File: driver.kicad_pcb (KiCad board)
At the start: 2 copper layers, 25 x 20 mm, 29 parts, among them J1 FAN_TACH, J2 FAN_PWM, J3 HF1004E, Q1 BSS138, U1 MP2315SGJ-Z

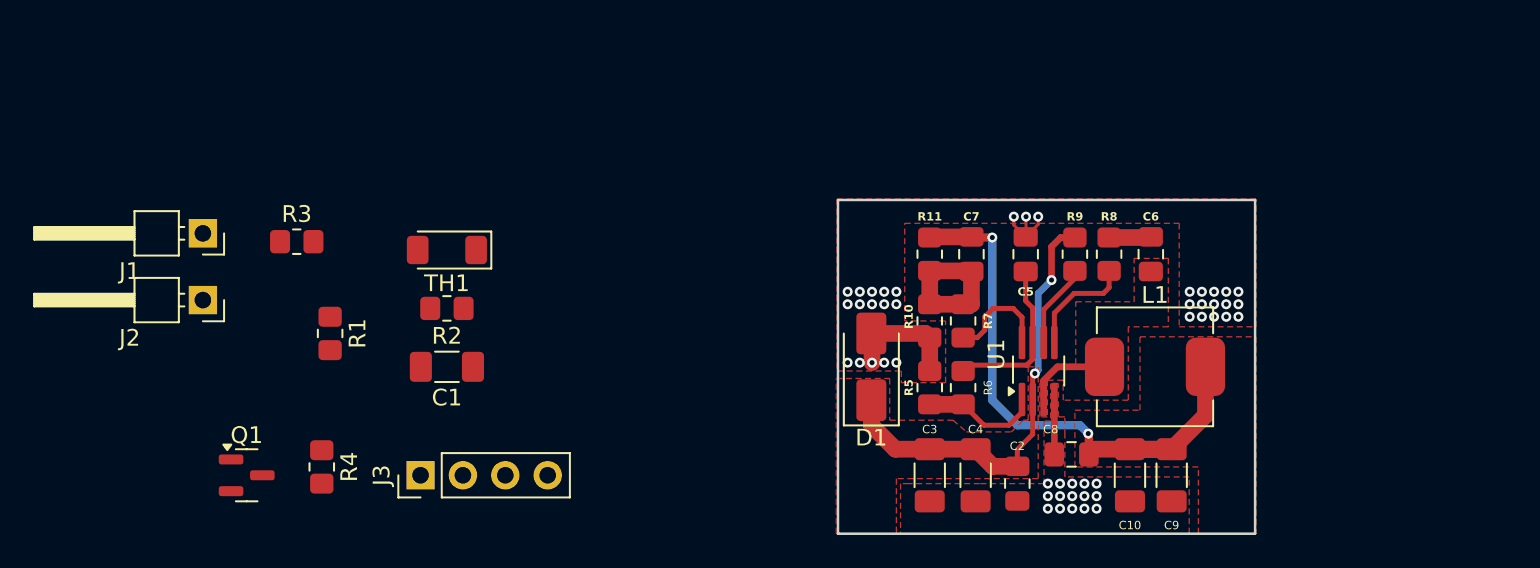
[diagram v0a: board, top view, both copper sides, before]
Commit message: add datasheet
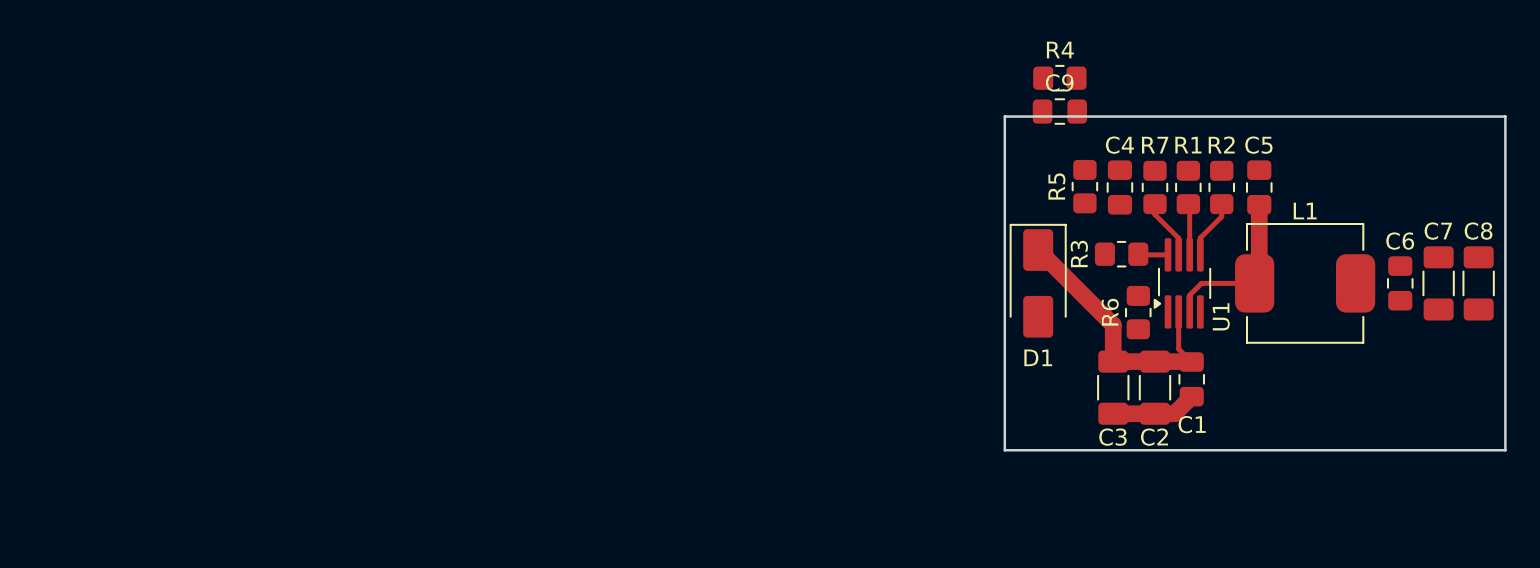
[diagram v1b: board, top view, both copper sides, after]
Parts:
- removed C10: 22uF, Capacitor_SMD:C_1206_3216Metric_Pad1.33x1.80mm_HandSolder
- removed J1: FAN_TACH, Connector_PinHeader_2.54mm:PinHeader_1x01_P2.54mm_Horizontal
- removed J2: FAN_PWM, Connector_PinHeader_2.54mm:PinHeader_1x01_P2.54mm_Horizontal
- removed J3: HF1004E, Connector_PinHeader_2.54mm:PinHeader_1x04_P2.54mm_Vertical
- removed Q1: BSS138, Package_TO_SOT_SMD:SOT-23
- removed R10: 7.5K, Resistor_SMD:R_0805_2012Metric_Pad1.20x1.40mm_HandSolder
- removed R11: 40.2K, Resistor_SMD:R_0805_2012Metric_Pad1.20x1.40mm_HandSolder
- removed R8: 10R, Resistor_SMD:R_0805_2012Metric_Pad1.20x1.40mm_HandSolder
- removed R9: 499K, Resistor_SMD:R_0805_2012Metric_Pad1.20x1.40mm_HandSolder
- removed TH1: KTY85, Diode_SMD:D_MiniMELF
- C1: value 25V 10uF -> 0.1uF; footprint Capacitor_SMD:C_1206_3216Metric_Pad1.33x1.80mm_HandSolder -> Capacitor_SMD:C_0805_2012Metric_Pad1.18x1.45mm_HandSolder
- C2, C8: value 0.1uF -> 22uF; footprint Capacitor_SMD:C_0805_2012Metric_Pad1.18x1.45mm_HandSolder -> Capacitor_SMD:C_1206_3216Metric_Pad1.33x1.80mm_HandSolder
- C4: value 22uF -> 0.1uF; footprint Capacitor_SMD:C_1206_3216Metric_Pad1.33x1.80mm_HandSolder -> Capacitor_SMD:C_0805_2012Metric_Pad1.18x1.45mm_HandSolder
- C7: value 33pF -> 22uF; footprint Capacitor_SMD:C_0805_2012Metric_Pad1.18x1.45mm_HandSolder -> Capacitor_SMD:C_1206_3216Metric_Pad1.33x1.80mm_HandSolder
- C9: value 22uF -> 33pF; footprint Capacitor_SMD:C_1206_3216Metric_Pad1.33x1.80mm_HandSolder -> Capacitor_SMD:C_0805_2012Metric_Pad1.18x1.45mm_HandSolder
- R1: value 2.2K -> 100K
- R2: value 4.7K -> 10R
- R3: value 27K -> 20K
- R4: value 10K -> 40.2K
- R5: value 9.09K -> 7.5K
- R6: value 100K -> 9.09K
- R7: value 20K -> 100K
- moved R1 52.2 mm to (131.0, 64.2)
- moved R4 50.0 mm to (123.3, 57.7), turned to 0 degrees
- moved R3 49.4 mm to (127.0, 68.2), turned to 180 degrees
- moved R2 47.0 mm to (133.0, 64.2), turned to 90 degrees
- moved C1 44.6 mm to (131.2, 75.8), turned to -90 degrees
- moved C7 28.1 mm to (146.0, 70.0), turned to -90 degrees
- moved C8 26.5 mm to (148.4, 70.0), turned to -90 degrees
- moved C9 22.8 mm to (123.3, 59.7), turned to 0 degrees
- moved C4 19.3 mm to (126.9, 64.2)
- moved R5 15.2 mm to (124.8, 64.2), turned to 90 degrees
- moved C6 15.1 mm to (143.7, 70.0)
- moved C5 14.6 mm to (135.2, 64.2)
- moved R7 14.0 mm to (129.0, 64.2)
- moved C3 12.2 mm to (126.5, 76.2)
- moved R6 11.4 mm to (128.0, 71.8), turned to 90 degrees
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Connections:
- C4 pad 1: +12V -> GND
- C4 pad 2: GND -> /VCC_MP2315
- C5 pad 1: GND -> Net-(C5-Pad1)
- C5 pad 2: /VCC_MP2315 -> /SW
- C6 pad 1: Net-(C6-Pad1) -> +5V
- C6 pad 2: /SW -> GND
- C7 pad 1: Net-(C7-Pad1) -> +5V
- C7 pad 2: +5V -> GND
- C9 pad 1: +5V -> Net-(C9-Pad1)
- C9 pad 2: GND -> +5V
- R1 pad 1: +5V -> +12V
- R1 pad 2: Net-(J3-Pin_1) -> /EN
- R2 pad 1: +12V -> /BST
- R2 pad 2: Net-(J3-Pin_2) -> Net-(C5-Pad1)
- R3 pad 1: Net-(J1-Pin_1) -> /FB
- R3 pad 2: Net-(J3-Pin_2) -> Net-(C9-Pad1)
- R4 pad 1: Net-(J1-Pin_1) -> Net-(C9-Pad1)
- R4 pad 2: GND -> +5V
- R5 pad 1: GND -> Net-(C9-Pad1)
- R5 pad 2: /AAM -> GND
- R6 pad 1: /VCC_MP2315 -> GND
- R7 pad 1: /FB -> /VCC_MP2315
- R7 pad 2: Net-(C7-Pad1) -> /AAM
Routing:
- net +5V: track 35.2 -> 0.00 mm, vias 2 -> 0
- net +12V: track 26.9 -> 16.6 mm, vias 2 -> 0
- net GND: track 15.0 -> 5.12 mm, vias 48 -> 0
- net Net-(C7-Pad1): track 8.98 -> 0.00 mm
- net /AAM: track 7.13 -> 0.00 mm
- net /VCC_MP2315: track 10.5 -> 3.63 mm
- net /FB: track 6.45 -> 1.80 mm
- net /BST: track 6.67 -> 3.57 mm
- net /SW: track 7.16 -> 10.0 mm
- net Net-(C6-Pad1): track 2.52 -> 0.00 mm
- net /EN: track 5.06 -> 3.07 mm
- removed copper zone on F.Cu, net +12V
- removed copper zone on F.Cu, net +5V
- removed copper zone on F.Cu, net /SW
- removed copper zone on B.Cu, net GND
- removed copper zone on F.Cu, net GND
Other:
- board size 25 x 20 mm -> 30 x 20 mm
